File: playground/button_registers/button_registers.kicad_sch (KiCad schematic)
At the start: 1 part, among them U1 74HC165

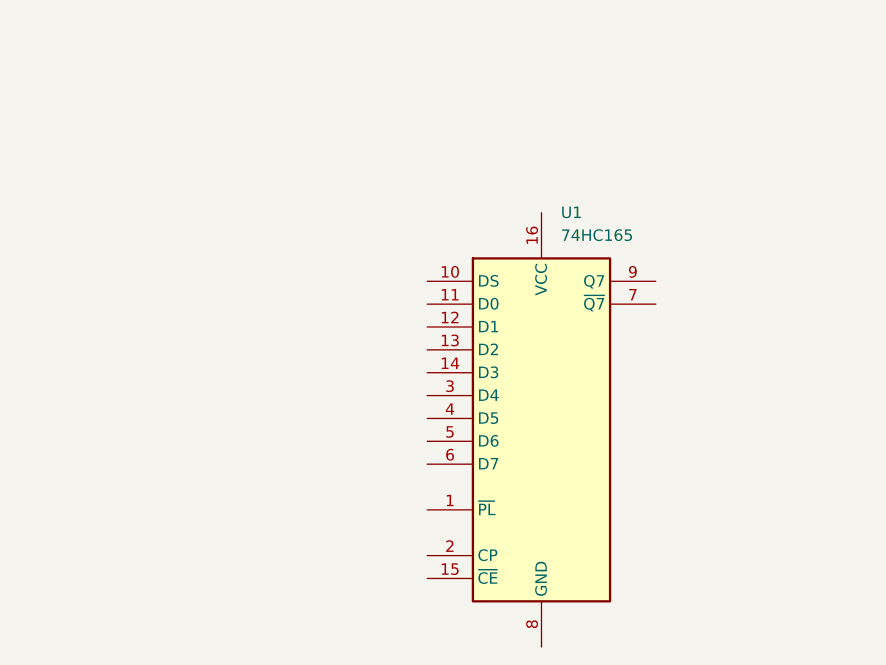
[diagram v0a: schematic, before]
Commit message: Set up correct output for performing test 1
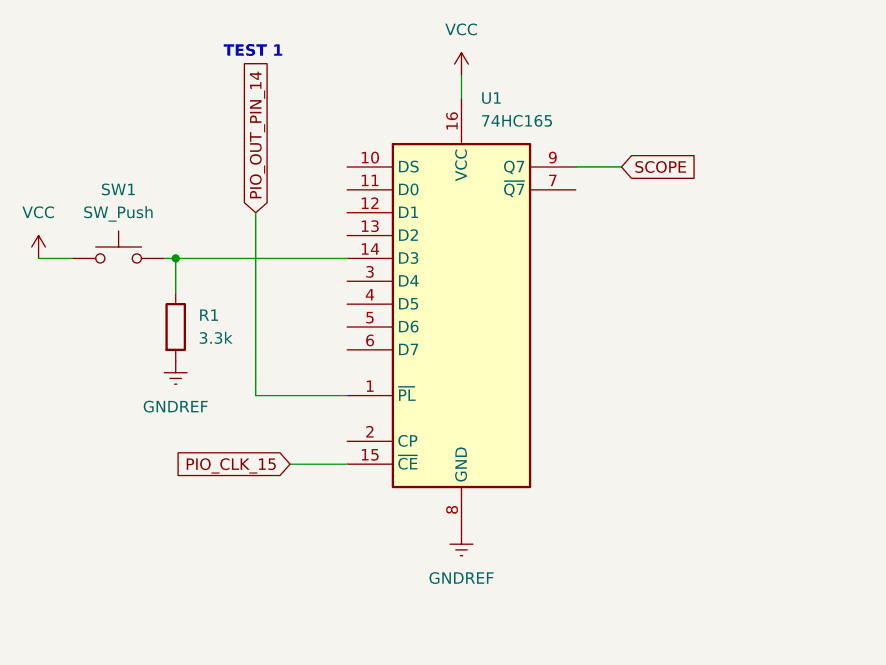
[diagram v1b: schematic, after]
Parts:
- added R1: 3.3k, symbol Device:R
- added SW1: SW_Push, symbol Switch:SW_Push
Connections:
- net PIO_OUT_PIN_14: now reaches U1.1 (~{PL})
- net at U1.14 (D3): now also R1.1, SW1.2
- net PIO_CLK_15: now reaches U1.15 (~{CE})
- net VCC: now reaches U1.16 (VCC)
- net VCC: now also SW1.1
- net GNDREF: now reaches U1.8 (GND)
- net GNDREF: now also R1.2
- net SCOPE: now reaches U1.9 (Q7)
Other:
- note added: "TEST 1"
- moved on the sheet: U1

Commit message: Added ground to serial in pin, test passed succesfully
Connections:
- net GNDREF: now also U1.10 (DS)
- net PIO_CLK_15: now also U1.2 (CP); no longer U1.15 (~{CE})
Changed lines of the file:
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@@
-	(wire
-		(pts
-			(xy 43.18 72.39) (xy 49.53 72.39)
-		)
-		(stroke
-			(width 0)
-			(type default)
-		)
-	)
 	(wire
 		(pts
@@
 		(pts
 			(xy 39.37 64.77) (xy 49.53 64.77)
+		)
+		(stroke
+			(width 0)
+			(type default)
+		)
+	)
+	(wire
+		(pts
+			(xy 40.64 69.85) (xy 49.53 69.85)
 		)
 		(stroke
@@
 	(global_label "PIO_CLK_15"
 		(shape input)
-		(at 43.18 72.39 180)
+		(at 40.64 69.85 180)
 		(fields_autoplaced yes)
 		(effects
@@
 		)
 		(property "Intersheetrefs" "${INTERSHEET_REFS}"
-			(at 29.0672 72.39 0)
+			(at 26.5272 69.85 0)
 			(effects
 				(font
@@
 					(unit 1)
 				)
+			)
+		)
+	)
+	(symbol
+		(lib_id "power:GNDREF")
+		(at 49.53 39.37 270)
+		(unit 1)
+		(exclude_from_sim no)
+		(in_bom yes)
+		(on_board yes)
+		(dnp no)
+		(fields_autoplaced yes)
+		(property "Reference" "#PWR05"
+			(at 43.18 39.37 0)
+			(effects
+				(font
+					(size 1.27 1.27)
+				)
+				(hide yes)
+			)
+		)
+		(property "Value" "GNDREF"
+			(at 45.72 39.3699 90)
+			(effects
+				(font
+					(size 1.27 1.27)
+				)
+				(justify right)
+			)
+		)
+		(property "Footprint" ""
+			(at 49.53 39.37 0)
+			(effects
+				(font
+					(size 1.27 1.27)
+				)
+				(hide yes)
+			)
+		)
+		(property "Datasheet" ""
+			(at 49.53 39.37 0)
+			(effects
+				(font
+					(size 1.27 1.27)
+				)
+				(hide yes)
+			)
+		)
+		(property "Description" "Power symbol creates a global label with name \"GNDREF\" , reference supply ground"
+			(at 49.53 39.37 0)
+			(effects
+				(font
+					(size 1.27 1.27)
+				)
+				(hide yes)
+			)
+		)
+		(pin "1"
+		)
+		(instances
+			(project ""
+				(path "/a0ef2865-da3e-4a7c-abf4-5bbeccf70e64"
+					(reference "#PWR05")
+					(unit 1)
+				)

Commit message: test 2 schematic
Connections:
- net SCOPE renamed PICO_INPUT_13
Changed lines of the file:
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@@
+		(color 0 0 0 0)
+	)
+	(junction
+		(at 77.47 39.37)
+		(diameter 0)
 		(color 0 0 0 0)
 	)
@@
 	(wire
 		(pts
-			(xy 74.93 39.37) (xy 80.01 39.37)
+			(xy 77.47 27.94) (xy 87.63 27.94)
+		)
+		(stroke
+			(width 0)
+			(type default)
+		)
+	)
+	(wire
+		(pts
+			(xy 74.93 39.37) (xy 77.47 39.37)
 		)
 		(stroke
@@
 		(pts
 			(xy 30.48 49.53) (xy 49.53 49.53)
+		)
+		(stroke
+			(width 0)
+			(type default)
+		)
+	)
+	(wire
+		(pts
+			(xy 77.47 39.37) (xy 77.47 27.94)
+		)
+		(stroke
+			(width 0)
+			(type default)
+		)
+	)
+	(wire
+		(pts
+			(xy 77.47 39.37) (xy 80.01 39.37)
 		)
 		(stroke
@@
 			(effects
 				(font
+					(size 1.27 1.27)
+				)
+				(justify left)
+				(hide yes)
+			)
+		)
+	)
+	(global_label "PICO_INPUT_13"
+		(shape input)
+		(at 87.63 27.94 0)
+		(fields_autoplaced yes)
+		(effects
+			(font
+				(size 1.27 1.27)
+			)
+			(justify left)
+		)
+		(property "Intersheetrefs" "${INTERSHEET_REFS}"
+			(at 104.9481 27.94 0)
+			(effects
+				(font

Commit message: Added important ground connection to CLK INH
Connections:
- net GNDREF: now also U1.15 (~{CE})
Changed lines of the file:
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@@
+	(wire
+		(pts
+			(xy 49.53 72.39) (xy 45.72 72.39)
+		)
+		(stroke
+			(width 0)
+			(type default)
+		)
+	)
 	(wire
 		(pts
@@
 		(pts
 			(xy 39.37 64.77) (xy 49.53 64.77)
+		)
+		(stroke
+			(width 0)
+			(type default)
+		)
+	)
+	(wire
+		(pts
+			(xy 45.72 72.39) (xy 45.72 74.93)
 		)
 		(stroke
@@
 					(unit 1)
 				)
+			)
+		)
+	)
+	(symbol
+		(lib_id "power:GNDREF")
+		(at 45.72 74.93 0)
+		(unit 1)
+		(exclude_from_sim no)
+		(in_bom yes)
+		(on_board yes)
+		(dnp no)
+		(fields_autoplaced yes)
+		(property "Reference" "#PWR06"
+			(at 45.72 81.28 0)
+			(effects
+				(font
+					(size 1.27 1.27)
+				)
+				(hide yes)
+			)
+		)
+		(property "Value" "GNDREF"
+			(at 45.72 80.01 0)
+			(effects
+				(font
+					(size 1.27 1.27)
+				)
+			)
+		)
+		(property "Footprint" ""
+			(at 45.72 74.93 0)
+			(effects
+				(font
+					(size 1.27 1.27)
+				)
+				(hide yes)
+			)
+		)
+		(property "Datasheet" ""
+			(at 45.72 74.93 0)
+			(effects
+				(font
+					(size 1.27 1.27)
+				)
+				(hide yes)
+			)
+		)
+		(property "Description" "Power symbol creates a global label with name \"GNDREF\" , reference supply ground"
+			(at 45.72 74.93 0)
+			(effects
+				(font
+					(size 1.27 1.27)
+				)
+				(hide yes)
+			)
+		)
+		(pin "1"
+		)
+		(instances
+			(project ""
+				(path "/a0ef2865-da3e-4a7c-abf4-5bbeccf70e64"
+					(reference "#PWR06")
+					(unit 1)
+				)
